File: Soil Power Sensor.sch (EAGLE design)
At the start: 53 parts, among them J1 12401832E402A, U10 TPS7A20330PDBVR, U11 TPS60403DBVR, U12 REF1933AIDDCR, U2 FT234XD-R, U3 MAX9944ATA+T, U5 LTC6362CDDPBF, U6 LTC6362CDDPBF, U7 INA296A5, U8 MAX11201AEUB+, U9 MAX11201AEUB+, X1 SMA-142-0701-801/806

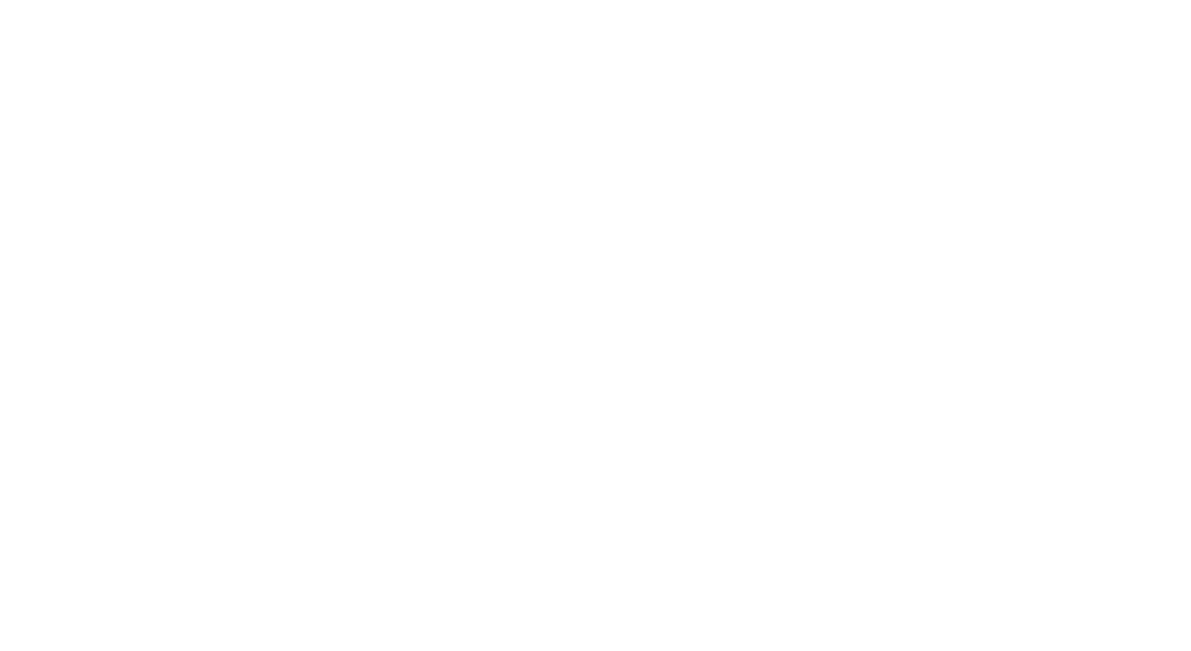
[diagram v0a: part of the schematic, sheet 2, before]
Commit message: Added battery with selectables jumpers
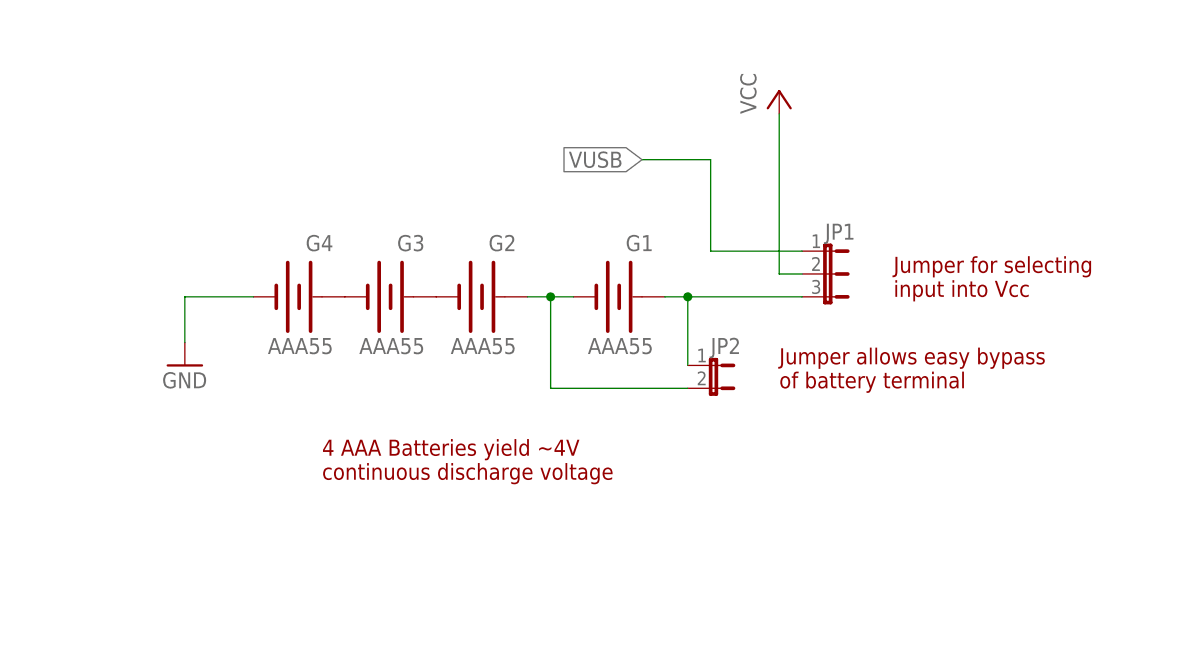
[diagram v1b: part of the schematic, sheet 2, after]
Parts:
- added G1, G2, G3, G4: AAA55, Soil Power Sensor:AAA55
- added JP1: (no value), jumper:JP2E
- added JP2: (no value), jumper:JP1E
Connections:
- new net N$16: G1.-, G2.+, JP2.2
- new net N$17: G2.-, G3.+
- new net N$18: G3.-, G4.+
- new net N$19: G1.+, JP1.3, JP2.1
- new net VUSB: E1.1, J1.VBUS1, J1.VBUS2, J1.VBUS3, J1.VBUS4, JP1.1
- net GND: now also G4.-
- net VCC: now also JP1.2; no longer E1.1, J1.VBUS1, J1.VBUS2, J1.VBUS3, J1.VBUS4
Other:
- note added: "4 AAA Batteries yield ~4V continuous discharge voltage"
- note added: "Jumper allows easy bypass of battery terminal"
- note added: "Jumper for selecting input into Vcc"

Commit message: Added Wifi Module (ESP32-C3)
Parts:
- added C10, C13: 0.1uF, rcl:C-EUC0603
- added C11: 1uF, rcl:C-EUC0603
- added C12: 10uF, rcl:C-EUC0603
- added C14, C15: NC, rcl:C-EUC0603
- added C8, C9: 1uF, rcl:C-EUC0805
- added JP3: JTAG, jumper:JP4E
- added JP4: Boot Option, jumper:JP1E
- added JP5: USB, jumper:JP1E
- added R22, R26, R27: 0, rcl:R-US_R0603
- added R23, R24, R25: 10k, rcl:R-US_R0603
- added S3: (no value), switch-omron:10-XX
- added U13: TLV1117LV33DCYR, Soil Power Sensor:TLV1117LV33DCYR
- added U4: ESP32-C3-MINI-1-N4, Soil Power Sensor:ESP32-C3-MINI-1-N4
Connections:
- new net ESP32_RXD0: U1.PA3, U4.RXD0
- new net ESP32_TXD0: U1.PA2, U4.TXD0
- new net IO4/TMS: JP3.1, U4.IO4
- new net IO5/TDI: JP3.2, U4.IO5
- new net IO6/TCK: JP3.3, U4.IO6
- new net IO7/TDO: JP3.4, U4.IO7
- new net IO9/BOOT: JP4.1, U4.IO9
- new net N$21: R24.1, U4.IO8
- new net N$22: C10.1, R22.1, S3.S, S3.S1
- new net N$23: R26.1, U4.IO18
- new net N$24: C11.1, R22.2, R23.1, U4.EN
- new net N$25: R25.1, U4.IO2
- new net N$26: R27.1, U4.IO19
- new net N$39: C14.1, JP5.1, R26.2
- new net N$40: C15.1, JP5.2, R27.2
- new net VUSB_3V3: C12.1, C13.1, C9.1, R23.2, R24.2, R25.2, U13.OUT, U4.3V3
- net GND: now also C10.2, C11.2, C12.2, C13.2, C14.2, C15.2, C8.2, C9.2, JP4.2, S3.P, S3.P1, U13.GND, U4.GND
- net VUSB: now also C8.1, U13.IN
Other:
- note added: "Capacitors only placed if needed"
- note added: "Capacitors placed close to 3V3 pin"
- note added: "Pulls EN to GND"
- note added: "Recommended values for RC delay on EN pin"

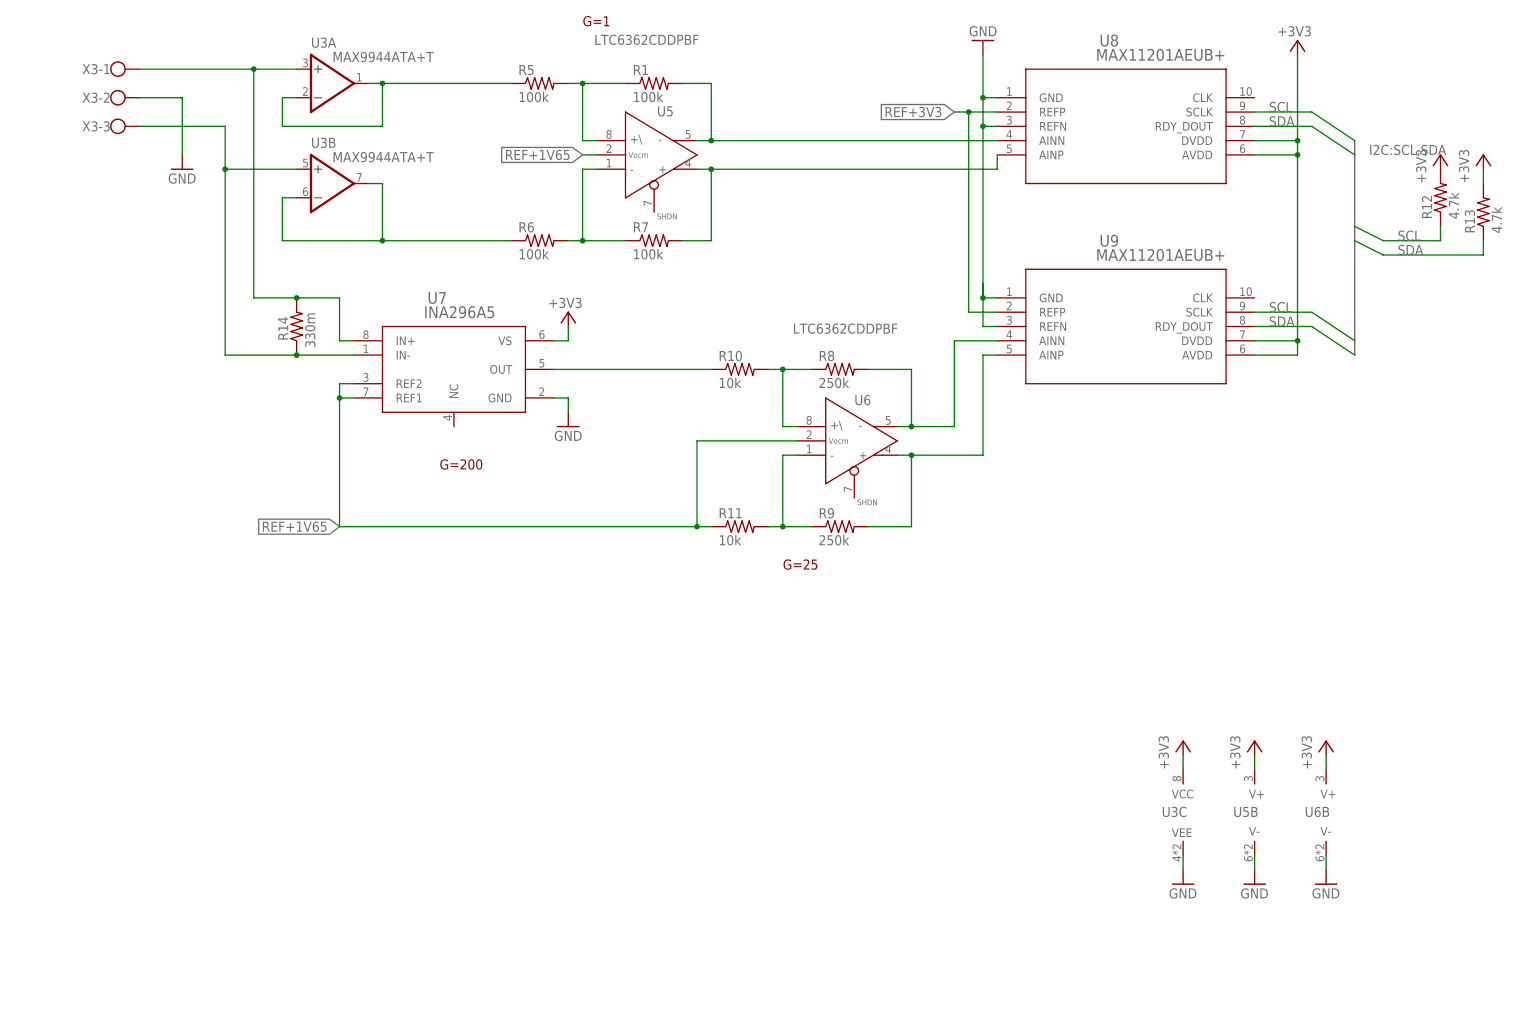
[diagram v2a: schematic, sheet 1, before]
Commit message: Fixed ADC interface with mux
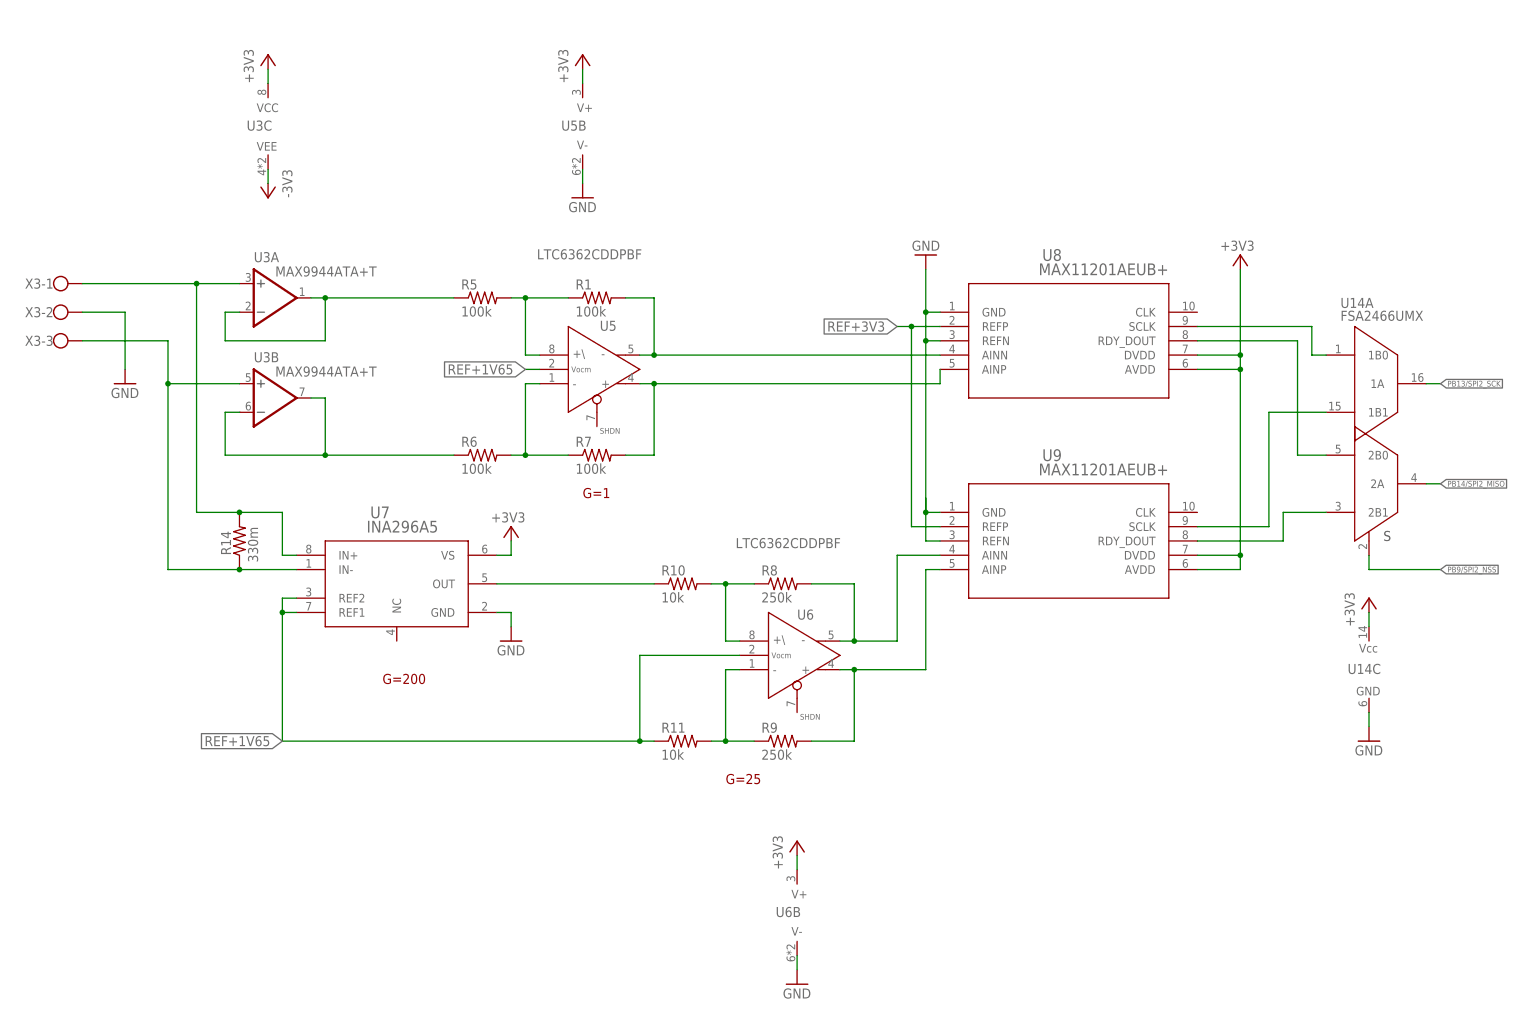
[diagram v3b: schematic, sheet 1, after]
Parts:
- removed R12, R13: 4.7k, rcl:R-US_R0402
- removed R3: 470, rcl:R-US_R0603
- removed S2: (no value), switch-omron:10-XX
- added U14: FSA2466UMX, Soil Power Sensor:FSA2466UMX
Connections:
- removed net N$5: R3.1, S2.S, S2.S1
- removed net PB13/BOOT/SCK: S2.P, S2.P1, U1.PB13
- removed net SCL: R12.1, U8.SCLK, U9.SCLK
- removed net SDA: R13.1, U8.RDY_DOUT, U9.RDY_DOUT
- new net N$41: U14A.1B0, U8.SCLK
- new net N$42: U14A.2B0, U8.RDY_DOUT
- new net N$43: U14A.1B1, U9.SCLK
- new net N$44: U14A.2B1, U9.RDY_DOUT
- new net PB13/SPI2_SCK: U1.PB13, U14A.1A
- new net PB14/SPI2_MISO: U1.PB14, U14A.2A
- new net PB9/SPI2_NSS: U1.PB9, U14A.S
- net +3V3: now also U14C.VCC; no longer R12.2, R13.2
- net -3V3: now also U3C.VEE
- net GND: now also U14C.GND; no longer R3.2, U3C.VEE
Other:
- moved on the sheet: R1, R10, R11, R14, R5, R6, R7, R8, R9, U3A, U3B, U3C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

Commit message: Fixed voltage and current connectors
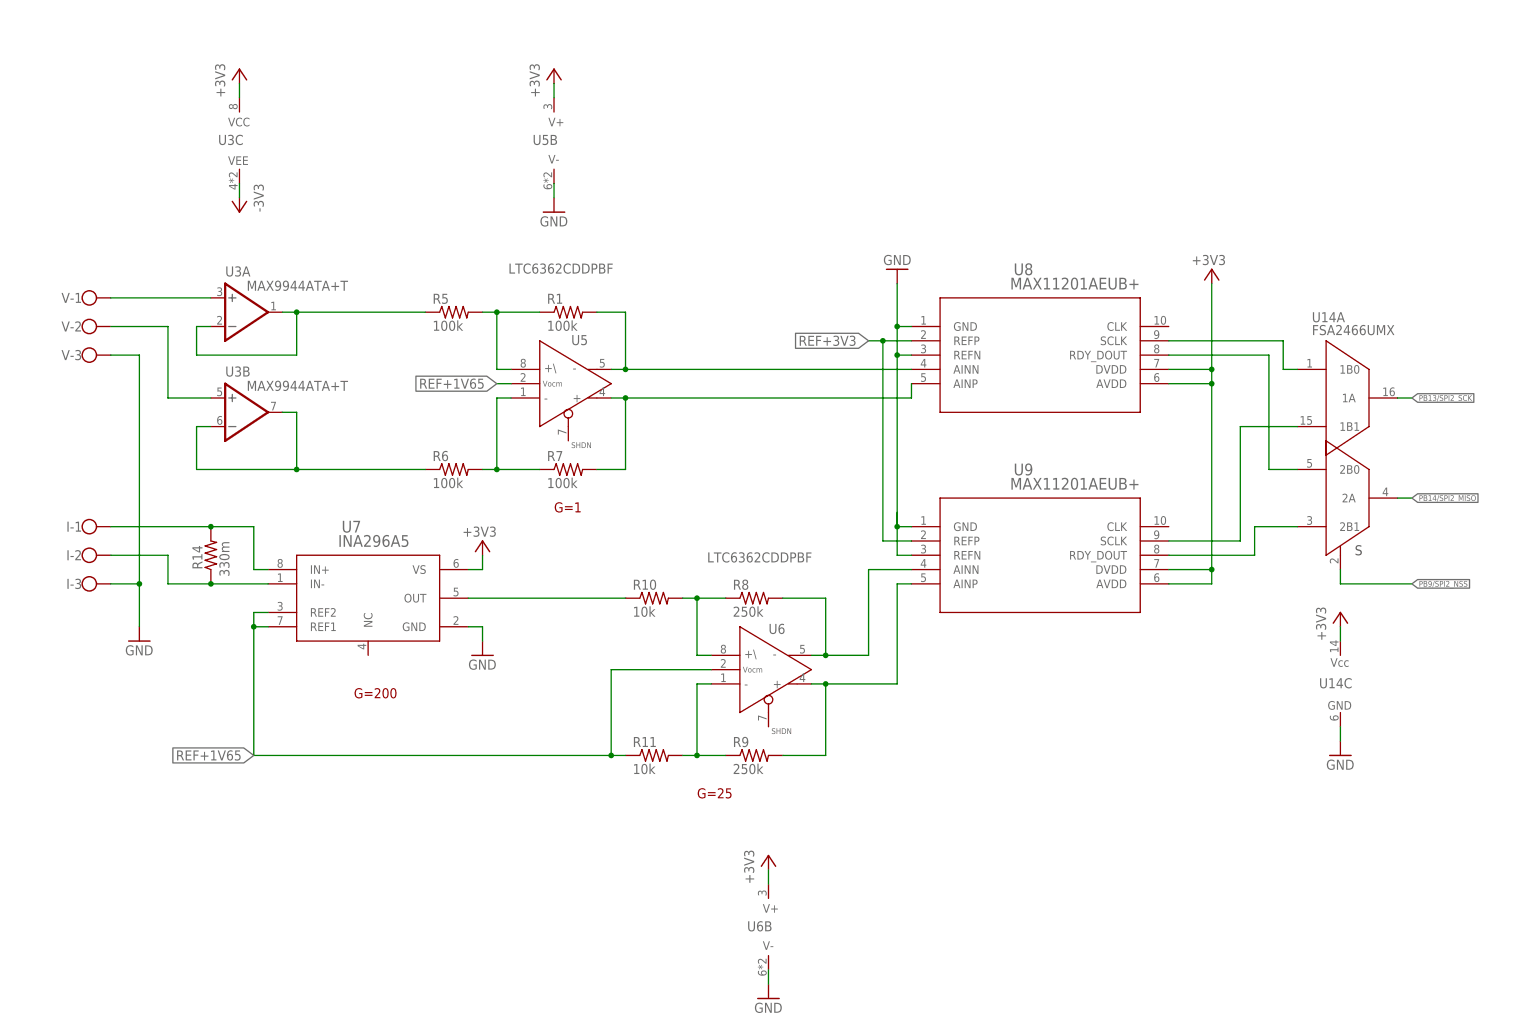
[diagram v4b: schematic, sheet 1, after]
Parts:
- removed X3: (no value), con-wago-500:W237-103
- added I, V: (no value), con-wago-500:W237-103
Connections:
- new net N$45: I-1.KL, R14.2, U7.IN+
- new net N$5: U3B.+IN, V-2.KL
- net GND: now also I-3.KL, V-3.KL; no longer X3-2.KL
- net N$1: now also V-1.KL; no longer R14.2, U7.IN+, X3-1.KL
- net N$38: now also I-2.KL; no longer U3B.+IN, X3-3.KL
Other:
- moved on the sheet: R1, R10, R11, R14, R5, R6, R7, R8, R9, U14A, U14C, U3A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
